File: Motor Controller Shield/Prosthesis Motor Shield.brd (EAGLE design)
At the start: 101.6 x 53.3 mm, 27 parts, among them M1_ACT M02PTH, M2_ACT M02PTH

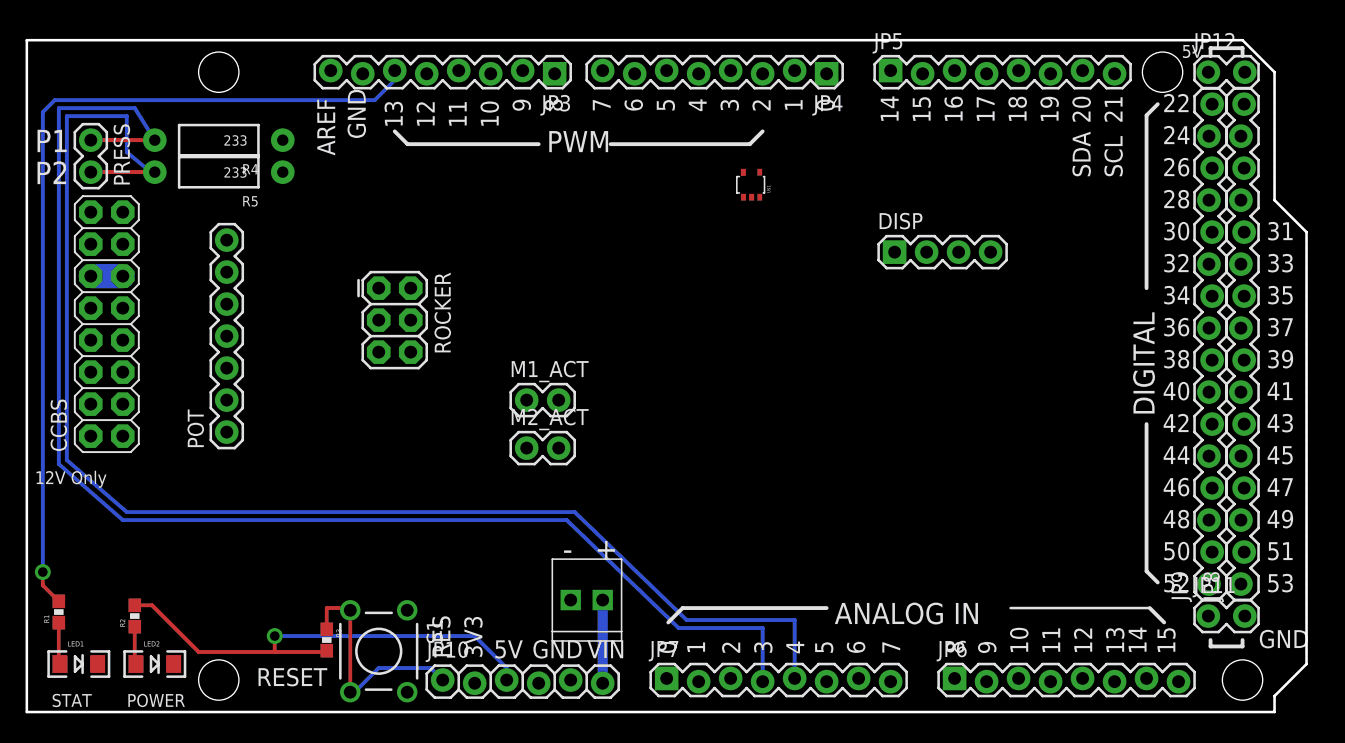
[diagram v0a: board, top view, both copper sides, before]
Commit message: Added additional HEX schmitt trigger inverters for debouncing.
Also fixed pin configurations in the MEGA shield. Some were backards.

Connected all of the pin headers to their respective components and
added debouncing for all switch signals.
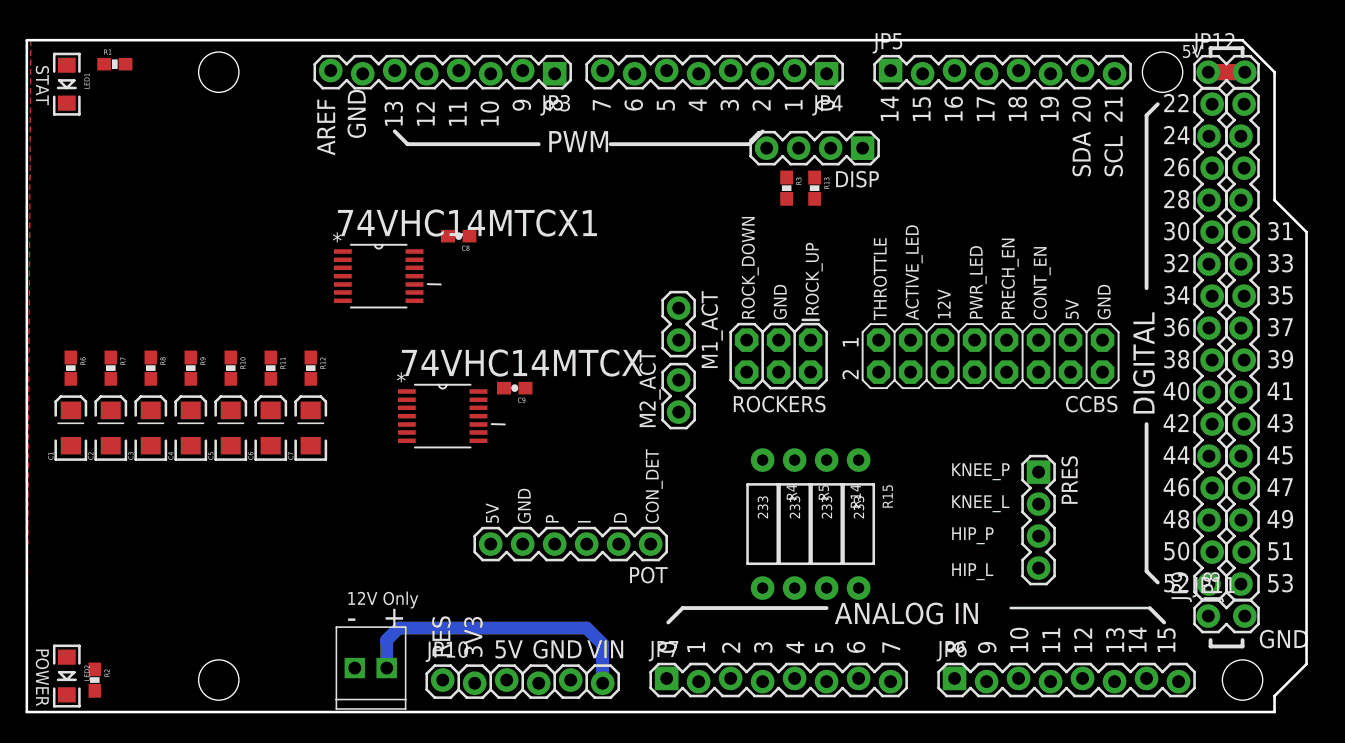
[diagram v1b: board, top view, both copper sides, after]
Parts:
- removed JP1: M022.54MM_SCREWTERM, SparkFun-Connectors:1X02_2.54_SCREWTERM
- removed PRESS: M02PTH, SparkFun-Connectors:1X02
- removed ROCKER: (no value), SparkFun-Connectors:2X3
- removed S1: (no value), SparkFun:TACTILE-PTH
- removed U$1: INVERTING_SCHMITT_TRIGGER, SparkFun-DigitalIC:TSSOP5
- added 74VHC14MTCX, 74VHC14MTCX1: 74VHC14MTCX, Fairchild_By_element14_Batch_1:SOP65P640X120-14N
- added C1, C2, C3, C4, C5: 0.1uF, SparkFun-Capacitors:EIA3216
- added C6, C7: (no value), SparkFun-Capacitors:EIA3216
- added C8, C9: 0.1uF, SparkFun-Capacitors:0603-CAP
- added PRES: (no value), SparkFun-Connectors:1X04
- added PWR: M022.54MM_SCREWTERM, SparkFun-Connectors:1X02_2.54_SCREWTERM
- added R10, R6, R7, R8, R9: 1M, SparkFun-Resistors:0603-RES
- added R11, R12: (no value), SparkFun-Resistors:0603-RES
- added R13: 3k, SparkFun-Resistors:0603-RES
- added R14, R15: 233, SparkFun-Resistors:AXIAL-0.4
- added ROCKERS: (no value), SparkFun-Connectors:2X3
- POT: device SparkFun-Connectors:1X07 -> SparkFun-Connectors:1X06
- R3: value 10k -> 3k; device SparkFun-Passives:0603-RES -> SparkFun-Resistors:0603-RES
- moved CCBS 78.2 mm to (85.4, 29.5), turned to 180 degrees
- moved R5 53.6 mm to (61.0, 14.9), turned to 270 degrees
- moved R4 52.9 mm to (58.4, 14.9), turned to 270 degrees
- moved R3 51.2 mm to (60.3, 41.6)
- moved LED1 46.0 mm to (3.17, 49.8), turned to 270 degrees
- moved R1 43.7 mm to (6.99, 51.4), turned to 0 degrees
- moved POT 34.8 mm to (49.5, 13.3), turned to 180 degrees
- moved M1_ACT 14.1 mm to (51.8, 32.1), turned to 270 degrees
- moved M2_ACT 12.4 mm to (51.8, 23.8), turned to 90 degrees
- moved DISP 8.64 mm to (66.4, 44.8), turned to 180 degrees
- moved LED2 7.05 mm to (3.17, 2.86), turned to 270 degrees
- moved R2 5.99 mm to (5.40, 2.54), turned to 270 degrees
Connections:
- removed net ACTIVE1_LED: CCBS.13
- removed net ACTIVE2_LED: CCBS.14
- removed net CONTACT1_EN: CCBS.5
- removed net CONTACT2_EN: CCBS.6
- removed net CON_SIG: POT.2
- removed net D: POT.3
- removed net I: POT.4
- removed net N$1: U$1.2
- removed net P: POT.5
- removed net PRECHARGE1_EN: CCBS.7
- removed net PRECHARGE2_EN: CCBS.8
- removed net PWR1_LED: CCBS.9
- removed net PWR_LED: CCBS.10
- removed net THROTTLE1: CCBS.15
- removed net THROTTLE2: CCBS.16
- new net M1_ACT_SIG_DET: 74VHC14MTCX.8
- new net M2_ACT_SIG_DET: 74VHC14MTCX1.2
- net 5V: now also 74VHC14MTCX.14, 74VHC14MTCX1.14, C8.2, C9.2, POT.6, R10.1, R11.1, R12.1, R13.1, R3.1, R6.1, R7.1, R8.1, R9.1; no longer CCBS.3, CCBS.4, M1_ACT.1, M2_ACT.1, POT.7, R3.2, ROCKER.3, ROCKER.4, U$1.5
- net 5V@1: now also CCBS.3, CCBS.4
- net A0: now also POT.4
- net A1: now also POT.3
- net A2: now also POT.2
- net A3: now also PRES.1; no longer PRESS.1
- net A4: now also PRES.2; no longer PRESS.2
- net A5: now also PRES.3, R14.P$2
- net A6: now also PRES.4, R15.P$2
- net CON_DET: now also 74VHC14MTCX.1, C1.A, R6.2
- net D11: now also CCBS.16
- net D12: now also CCBS.15
- net D14: now also JP5.1; no longer JP5.8
- net D15: now also JP5.2; no longer JP5.7
- net D16: now also JP5.3; no longer JP5.6
- net D17: now also JP5.4; no longer JP5.5
- net D18: now also JP5.5; no longer JP5.4
- net D19: now also JP5.6; no longer JP5.3
- net D2: now also 74VHC14MTCX.2; no longer U$1.4
- net D22: now also JP9.16; no longer JP9.1
- net D24: now also JP9.15; no longer JP9.2
- net D26: now also JP9.14; no longer JP9.3
- net D28: now also CCBS.13, JP9.13; no longer JP9.4
- net D30: now also CCBS.9, JP9.12; no longer JP9.5
- net D32: now also CCBS.7, JP9.11; no longer JP9.6
- net D34: now also CCBS.5, JP9.10; no longer JP9.7
- net D36: now also JP9.9; no longer JP9.8
- net D38: now also JP9.8; no longer JP9.9
- net D4: now also 74VHC14MTCX.4
- net D40: now also CCBS.6, JP9.7; no longer JP9.10
- net D42: now also CCBS.8, JP9.6; no longer JP9.11
- net D44: now also CCBS.10, JP9.5; no longer JP9.12
- net D46: now also CCBS.14, JP9.4; no longer JP9.13
- net D48: now also JP9.3; no longer JP9.14
- net D5: now also 74VHC14MTCX.12
- net D50: now also JP9.2; no longer JP9.15
- net D52: now also JP9.1; no longer JP9.16
- net D6: now also 74VHC14MTCX.6
- net D7: now also 74VHC14MTCX.10
- net GND: now also 74VHC14MTCX.7, 74VHC14MTCX1.7, C1.C, C2.C, C3.C, C4.C, C5.C, C6.C, C7.C, C8.1, C9.1, M1_ACT.1, M2_ACT.1, POT.5, PWR.P1, R14.P$1, R15.P$1, ROCKERS.3, ROCKERS.4; no longer JP1.P1, POT.6, S1.1, S1.2, U$1.3
- net M1_ACT_SIG: now also 74VHC14MTCX.9, C6.A, R11.2
- net M2_ACT_SIG: now also 74VHC14MTCX1.1, C7.A, R12.2
- net MOT1_ROCK_DOWN: now also 74VHC14MTCX.5, C3.A, R8.2, ROCKERS.5; no longer ROCKER.5
- net MOT1_ROCK_UP: now also 74VHC14MTCX.3, C2.A, R7.2, ROCKERS.1; no longer ROCKER.1
- net MOT2_ROCK_DOWN: now also 74VHC14MTCX.11, C5.A, R10.2, ROCKERS.6; no longer ROCKER.6
- net MOT2_ROCK_UP: now also 74VHC14MTCX.13, C4.A, R9.2, ROCKERS.2; no longer ROCKER.2
- net RES: no longer R3.1, S1.3, S1.4
- net SCL: now also JP5.8, R13.2; no longer JP5.1
- net SDA: now also JP5.7, R3.2; no longer JP5.2
- net VIN: now also PWR.P2; no longer JP1.P2
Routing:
- net A4: track 110.2 -> 0.00 mm
- net A3: track 107.6 -> 0.00 mm
- net D13: track 69.1 -> 0.00 mm, vias 1 -> 0
- net 5V: track 38.5 -> 0.00 mm, vias 1 -> 0
- net RES: track 18.7 -> 0.00 mm
- net VIN: track 9.14 -> 23.4 mm
- net 5V@1: track 0.00 -> 5.93 mm
- net N$127: track 3.31 -> 0.00 mm
- net N$126: track 3.00 -> 0.00 mm
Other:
- board text added: "12V"
- board text added: "ACTIVE_LED"
- board text added: "CONT_EN"
- board text added: "CON_DET"
- board text added: "D"
- board text added: "HIP_L"
- board text added: "HIP_P"
- board text added: "I"
- board text added: "KNEE_L"
- board text added: "KNEE_P"
- board text added: "P"
- board text added: "PRECH_EN"
- board text added: "PWR_LED"
- board text added: "ROCK_DOWN"
- board text added: "ROCK_UP"
- board text added: "THROTTLE"
- board text removed: "P1"
- board text removed: "P2"
- board text removed: "RESET"

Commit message: Incremental changes for layout.
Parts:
- moved C8 25.7 mm to (21.9, 15.2)
- moved 74VHC14MTCX1 24.5 mm to (15.9, 13.3)
- moved 74VHC14MTCX 21.7 mm to (16.2, 37.1)
- moved C9 21.4 mm to (22.2, 39.4)
- moved C4 21.3 mm to (28.3, 37.5), turned to 180 degrees
- moved DISP 20.1 mm to (50.8, 32.1)
- moved C1 19.9 mm to (6.35, 42.2), turned to 0 degrees
- moved R9 19.1 mm to (27.6, 39.7), turned to 180 degrees
- moved M2_ACT 19.1 mm to (32.7, 24.4), turned to 0 degrees
- moved M1_ACT 19.0 mm to (32.7, 32.1), turned to 0 degrees
- moved R12 18.2 mm to (6.99, 17.8), turned to 0 degrees
- moved C7 17.8 mm to (6.35, 15.2), turned to 0 degrees
- moved R6 17.5 mm to (6.99, 44.5), turned to 0 degrees
- moved R13 16.0 mm to (46.7, 39.7), turned to 0 degrees
- moved POT 14.2 mm to (40.6, 24.4), turned to 0 degrees
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- renumbered PRES to PRES_INPUT
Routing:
- net 5V: track 0.00 -> 82.8 mm, vias 0 -> 4
- net A3: track 0.00 -> 35.8 mm
- net A4: track 0.00 -> 32.3 mm
- net D46: track 0.00 -> 28.7 mm
- net 5V@1: track 5.93 -> 34.3 mm
- net A5: track 0.00 -> 27.6 mm
- net D13: track 0.00 -> 26.8 mm
- net D44: track 0.00 -> 22.7 mm
- net A6: track 0.00 -> 22.1 mm
- net D42: track 0.00 -> 18.8 mm
- net D40: track 0.00 -> 15.9 mm
- net MOT1_ROCK_DOWN: track 0.00 -> 10.8 mm
- net MOT2_ROCK_UP: track 0.00 -> 10.5 mm
- net CON_DET: track 0.00 -> 9.15 mm
- net MOT1_ROCK_UP: track 0.00 -> 7.89 mm
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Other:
- board text added: "SIG"

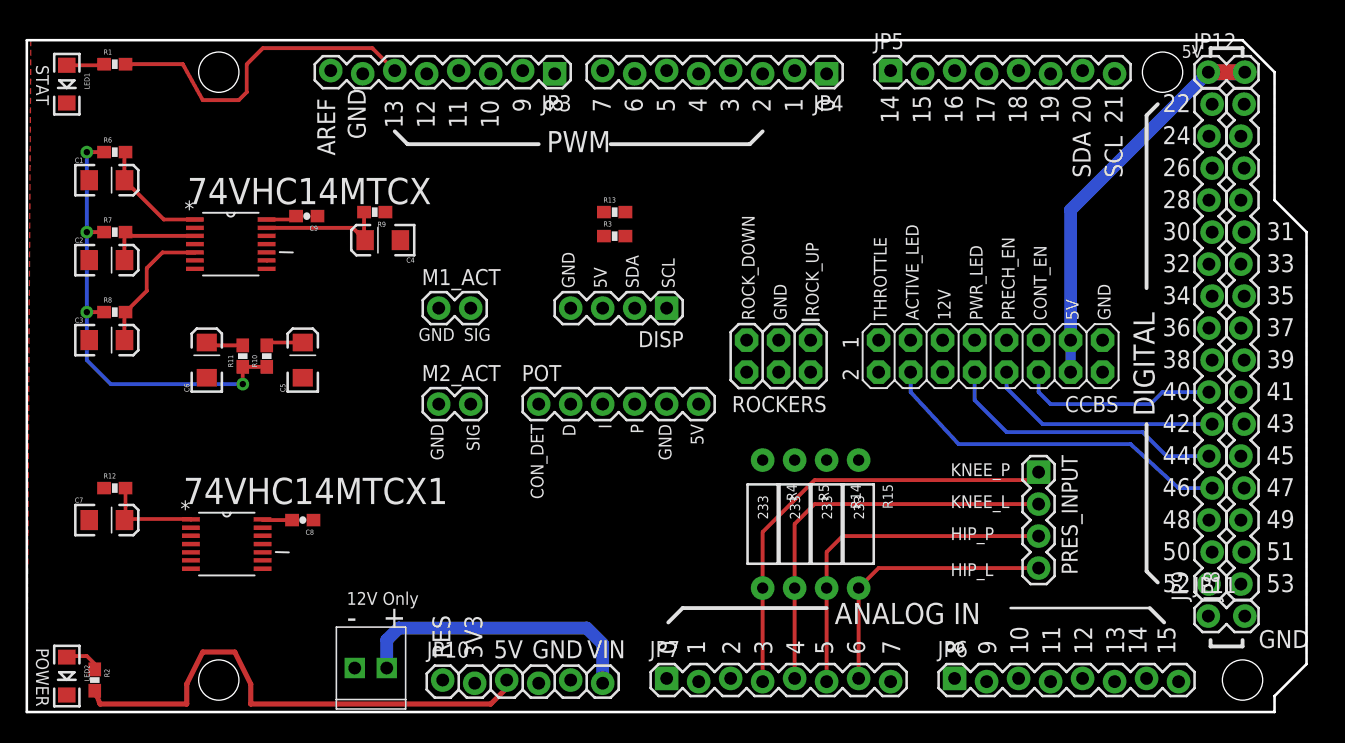
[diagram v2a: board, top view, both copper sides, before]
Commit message: Splitting M1 and M2 debouncing signals between the inverters
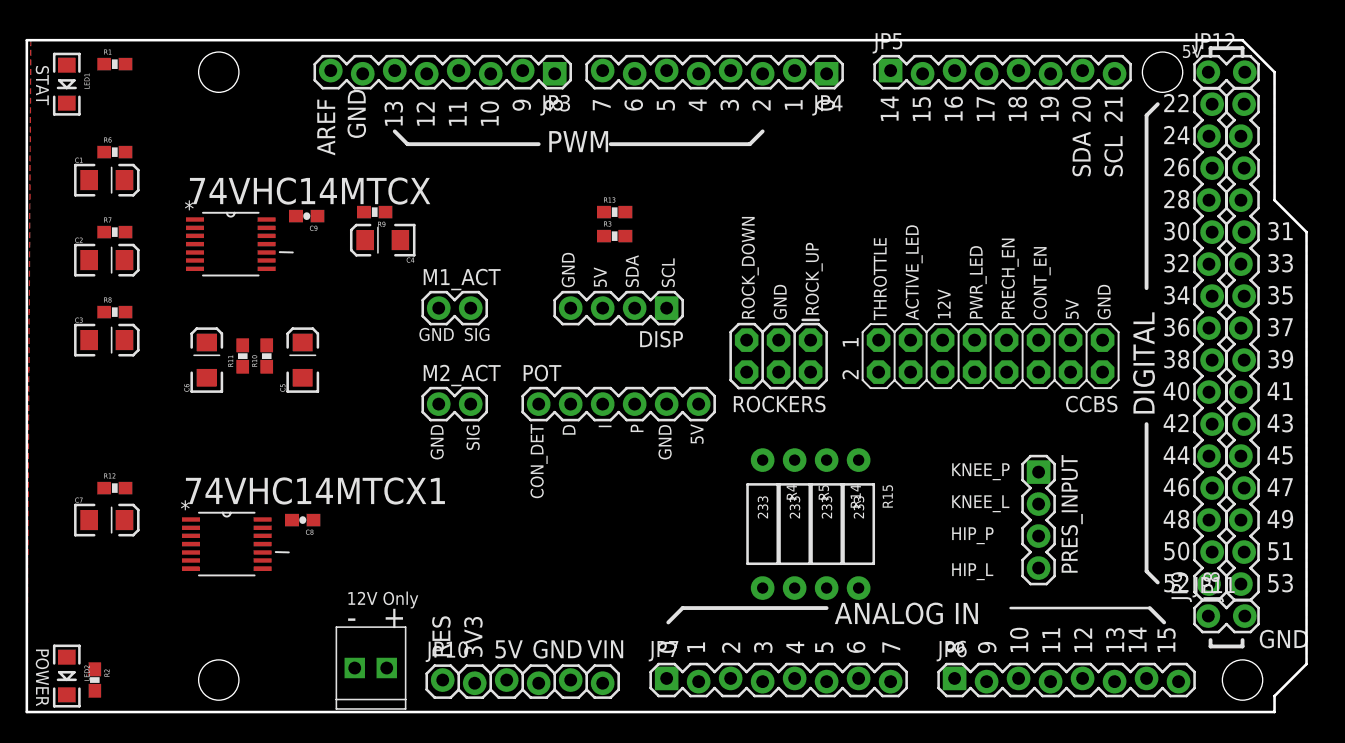
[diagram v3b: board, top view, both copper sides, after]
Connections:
- removed net M1_ACT_SIG_DET: 74VHC14MTCX.8
- removed net M2_ACT_SIG_DET: 74VHC14MTCX1.2
- net D26: now also 74VHC14MTCX.8
- net D48: now also 74VHC14MTCX1.2
- net D5: now also 74VHC14MTCX1.4; no longer 74VHC14MTCX.12
- net D7: now also 74VHC14MTCX1.6; no longer 74VHC14MTCX.10
- net MOT2_ROCK_DOWN: now also 74VHC14MTCX1.5; no longer 74VHC14MTCX.11
- net MOT2_ROCK_UP: now also 74VHC14MTCX1.3; no longer 74VHC14MTCX.13
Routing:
- net 5V: track 82.8 -> 0.00 mm, vias 4 -> 0
- net A3: track 35.8 -> 0.00 mm
- net 5V@1: track 34.3 -> 0.00 mm
- net A4: track 32.3 -> 0.00 mm
- net D46: track 28.7 -> 0.00 mm
- net A5: track 27.6 -> 0.00 mm
- net D13: track 26.8 -> 0.00 mm
- net VIN: track 23.4 -> 0.00 mm
- net D44: track 22.7 -> 0.00 mm
- net A6: track 22.1 -> 0.00 mm
- net D42: track 18.8 -> 0.00 mm
- net D40: track 15.9 -> 0.00 mm
- net MOT1_ROCK_DOWN: track 10.8 -> 0.00 mm
- net MOT2_ROCK_UP: track 10.5 -> 0.00 mm
- net CON_DET: track 9.15 -> 0.00 mm
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
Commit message: Routed motor controller arduino shield. Challenging!
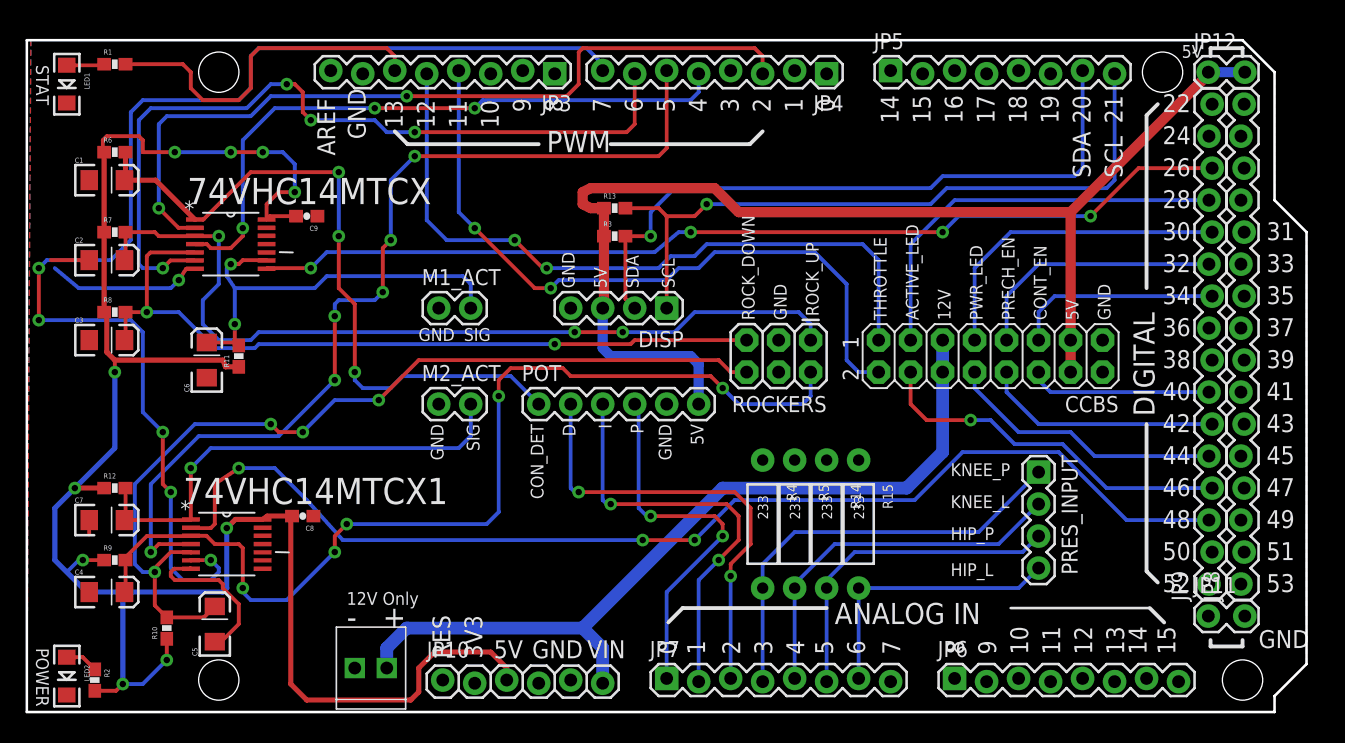
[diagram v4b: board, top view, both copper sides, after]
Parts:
- moved C4 35.5 mm to (6.35, 9.53), turned to 0 degrees
- moved R9 34.5 mm to (6.99, 12.1), turned to 0 degrees
- moved R10 23.0 mm to (11.1, 6.67)
- moved C5 22.1 mm to (14.9, 6.99)
- moved R13 0.32 mm to (46.7, 40.0)
- moved C8 0.32 mm to (21.9, 15.6)
- moved R11 0.32 mm to (16.8, 28.3)
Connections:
- net 5V: no longer DISP.3, POT.6, R13.1, R3.1
- net 5V@1: now also DISP.3, POT.6, R13.1, R3.1
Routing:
- net 5V: track 0.00 -> 153.0 mm, vias 0 -> 10
- net D7: track 0.00 -> 100.2 mm, vias 0 -> 5
- net 5V@1: track 0.00 -> 96.0 mm
- net D48: track 0.00 -> 92.1 mm, vias 0 -> 3
- net MOT2_ROCK_UP: track 0.00 -> 79.9 mm, vias 0 -> 5
- net D26: track 0.00 -> 78.3 mm, vias 0 -> 4
- net D5: track 0.00 -> 75.4 mm, vias 0 -> 6
- net MOT2_ROCK_DOWN: track 0.00 -> 73.7 mm, vias 0 -> 4
- net MOT1_ROCK_UP: track 0.00 -> 68.7 mm, vias 0 -> 3
- net VIN: track 0.00 -> 66.1 mm
- net D2: track 0.00 -> 63.8 mm, vias 0 -> 2
- net D6: track 0.00 -> 63.6 mm, vias 0 -> 4
- net MOT1_ROCK_DOWN: track 0.00 -> 61.4 mm, vias 0 -> 2
- net D12: track 0.00 -> 56.7 mm, vias 0 -> 2
- net SCL: track 0.00 -> 56.0 mm, vias 0 -> 1
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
